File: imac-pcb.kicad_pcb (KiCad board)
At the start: 2 copper layers, 43 parts, among them P2 PATCHBAY_IO, P5 INPUTS, P7 PWR_X3, Q1 NX3008N***, Q2 PMV48XP, Q3 NX3008N***, Q4 NX3008N***, U1 MCP6004, U2 MCP6004, U3 NCP4620, U4 ADG849

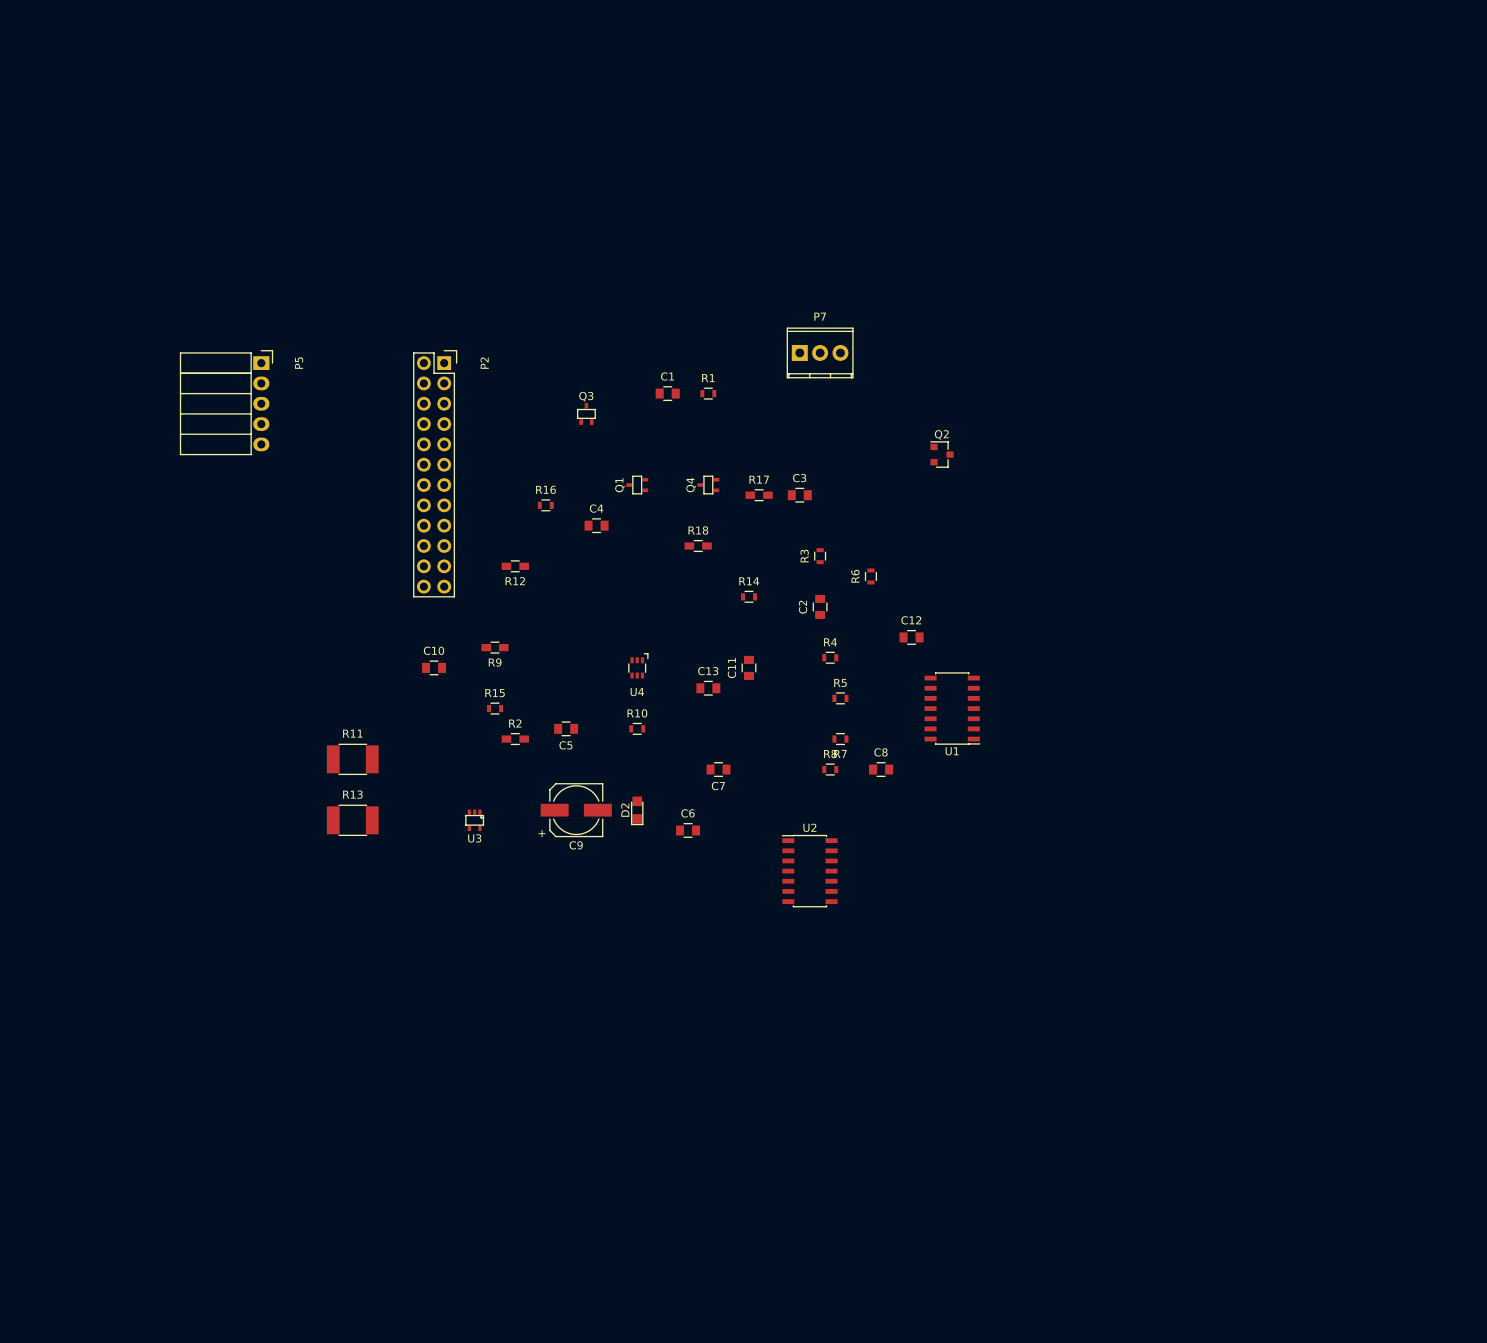
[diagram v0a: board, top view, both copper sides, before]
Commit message: begin layout of pcb
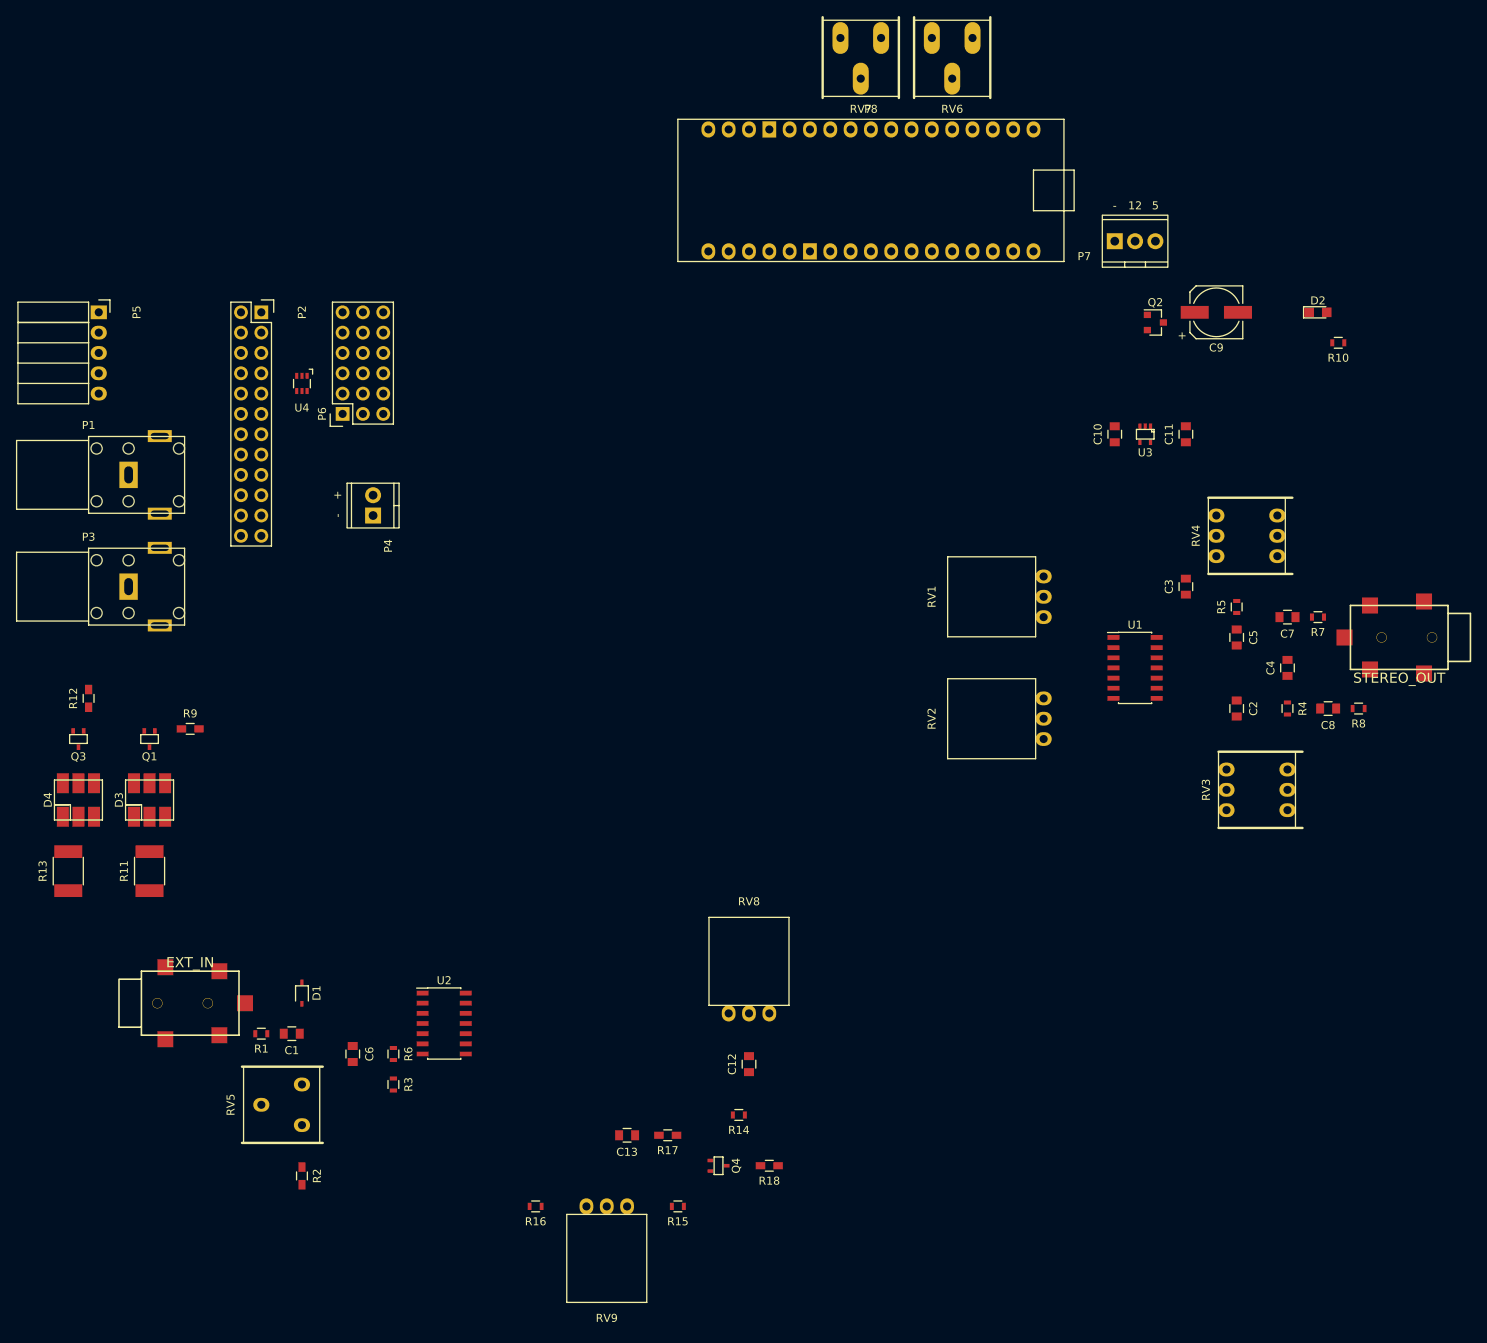
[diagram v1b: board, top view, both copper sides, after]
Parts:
- added D1: 1N4148, Imac:SOD-323F, F.Cu at (114.3, 151.1)
- added D3: CLP6B-WKW, Imac:PLCC6-3in1-SMD-LED, F.Cu at (95.2, 127.0)
- added D4: CLP6B-WKW, Imac:PLCC6-3in1-SMD-LED, F.Cu at (86.4, 127.0)
- added J1: EXT_IN, Lumberg:Lumberg_1503_03, F.Cu at (100.3, 152.4)
- added J2: STEREO_OUT, Lumberg:Lumberg_1503_03, F.Cu at (251.5, 106.7)
- added P1: PROBE1, Imac:PSG01546_RCA_Phono_Connector, F.Cu at (87.6, 86.4)
- added P3: PROBE2, Imac:PSG01546_RCA_Phono_Connector, F.Cu at (87.6, 100.3)
- added P4: EXT_OUT, Imac:TerminalBlock_TE_282834-2-2.54mm_2pol, F.Cu at (123.2, 91.4)
- added P6: PATCHBAY_A, Imac:Socket_Strip_Straight_3x06, F.Cu at (119.4, 78.7)
- added P8: ARDUINO_MICRO, Imac:Arduino_Micro_2x1x17, F.Cu at (165.1, 43.2)
- added RV1: 100k, Imac:Pot_Bourns_PTV09A-4_Horizontal_Rear_mount, F.Cu at (207.0, 104.1)
- added RV2: 100k, Imac:Pot_Bourns_PTV09A-4_Horizontal_Rear_mount, F.Cu at (207.0, 119.4)
- added RV3: 100k, Imac:Dual_Pot_Bourns_3301H-00X, F.Cu at (229.9, 128.3)
- added RV4: 100k, Imac:Dual_Pot_Bourns_3301H-00X, F.Cu at (228.6, 96.5)
- added RV5: 100k**, Imac:Trimpot_Bourns_3386F_Vishay_M63, F.Cu at (114.3, 167.6)
- added RV6: 100k†, Imac:Trimpot_Bourns_Big_Pads_3386F_Vishay_M63, F.Cu at (198.1, 31.8)
- added RV7: 100k†, Imac:Trimpot_Bourns_Big_Pads_3386F_Vishay_M63, F.Cu at (186.7, 31.8)
- added RV8: 100k, Imac:Pot_Bourns_PTV09A-4_Horizontal_Rear_mount, F.Cu at (167.6, 153.7)
- added RV9: 100k, Imac:Pot_Bourns_PTV09A-4_Horizontal_Rear_mount, F.Cu at (154.9, 177.8)
- P7: footprint Terminal_Blocks:TerminalBlock_Pheonix_MPT-2.54mm_3pol -> Imac:TerminalBlock_TE_282834-3-2.54mm_3pol
- moved D2 105.4 mm to (241.3, 66.0), turned to 0 degrees
- moved C9 101.4 mm to (228.6, 66.0)
- moved R10 100.0 mm to (243.8, 69.8), turned to 180 degrees
- moved R1 97.6 mm to (109.2, 156.2), turned to 180 degrees
- moved U3 96.7 mm to (219.7, 81.3)
- moved C1 92.8 mm to (113.0, 156.2), turned to 180 degrees
- moved C10 90.0 mm to (215.9, 81.3), turned to 90 degrees
- moved C4 88.2 mm to (237.5, 110.5), turned to 90 degrees
- moved R16 87.6 mm to (143.5, 177.8), turned to 180 degrees
- moved Q4 85.1 mm to (166.4, 172.7), turned to 270 degrees
- moved R3 84.9 mm to (125.7, 162.6), turned to 270 degrees
- moved C5 84.6 mm to (231.1, 106.7), turned to 270 degrees
- moved R6 84.4 mm to (125.7, 158.8), turned to 270 degrees
- moved R17 80.8 mm to (160.0, 168.9), turned to 180 degrees
- moved R18 78.0 mm to (172.7, 172.7), turned to 180 degrees
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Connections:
- P2 pad 1: /PB1 -> /AUDIOA_SEND
- P2 pad 10: /D6 -> /IN3
- P2 pad 11: GND -> /AUDIOB_SEND
- P2 pad 12: GND -> /IN4
- P2 pad 13: /AUDIOA_SEND -> /LED_CTRL1
- P2 pad 14: /AUDIOA_SEND -> /IN5
- P2 pad 15: /AUDIOA_SEND -> /LED_CTRL2
- P2 pad 16: /AUDIOB_SEND -> /EXT_IN
- P2 pad 17: /AUDIOB_SEND -> /EXT_OUT
- P2 pad 18: /AUDIOB_SEND -> /D3
- P2 pad 19: /LED_CTRL1 -> /A0_IN
- P2 pad 2: /PB2 -> /PB1
- P2 pad 20: /LED_CTRL2 -> /D6
- P2 pad 21: /EXT_OUT -> GND
- P2 pad 22: /A0_IN -> GND
- P2 pad 3: /IN1 -> /AUDIOA_SEND
- P2 pad 4: /IN2 -> /PB2
- P2 pad 5: /IN3 -> /AUDIOA_SEND
- P2 pad 6: /IN4 -> /IN1
- P2 pad 7: /IN5 -> /AUDIOB_SEND
- P2 pad 8: /EXT_IN -> /IN2
- P2 pad 9: /D3 -> /AUDIOB_SEND

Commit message: major work on PCB layout
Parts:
- removed P8: ARDUINO_MICRO, Imac:Arduino_Micro_2x1x17
- added C14: 1u, Capacitors_SMD:C_0805, F.Cu at (71.8, -0.64)
- added C15: 100n, Capacitors_SMD:C_0805, F.Cu at (68.6, -0.64)
- added C16: 100n, Capacitors_SMD:C_0805, F.Cu at (83.8, -0.64)
- added C17: 1u, Capacitors_SMD:C_0805, F.Cu at (87.0, -0.64)
- added C18: 22u, Imac:2917C, F.Cu at (62.9, -0.64)
- added C19: 100n, Capacitors_SMD:C_0805, F.Cu at (64.3, 34.9)
- added C20: 100n, Capacitors_SMD:C_0805, F.Cu at (31.4, 16.4)
- added D5: CLP6B-WKW, Imac:PLCC6-3in1-SMD-LED, F.Cu at (43.3, 40.5)
- added R19: 27****, Resistors_SMD:R_1812_HandSoldering, F.Cu at (43.4, 34.6)
- added SW1: RESET_SW, Imac:EVQ_BUT, F.Cu at (66.7, 14.3)
- added U5: arduino_pro_micro, Imac:arduino_pro_micro, F.Cu at (74.3, -0.64)
- added U6: NCP1117-5, TO_SOT_Packages_SMD:SOT-223, F.Cu at (77.5, -0.64)
- C6: footprint Capacitors_SMD:C_0805 -> Capacitors_SMD:C_0805_HandSoldering
- D3, D4: moved to B.Cu
- Q1, Q3, Q4: footprint TO_SOT_Packages_SMD:SC-70 -> imac:SC-70-BIG-PADS
- R1, R10, R14, R15, R16, R3, R4, R5, R6, R7, R8: footprint Resistors_SMD:R_0603 -> Resistors_SMD:R_0805
- R11: value 27 -> 27****; footprint Resistors_SMD:R_1812 -> Resistors_SMD:R_1812_HandSoldering
- R12, R17, R18, R2, R9: footprint Resistors_SMD:R_0603_HandSoldering -> Resistors_SMD:R_0805_HandSoldering
- U2: value MCP6004 -> MCP6002; footprint Housings_SOIC:SOIC-14_3.9x8.7mm_Pitch1.27mm -> Imac:SOIC-8_3.9x4.9mm_Pitch1.27mm_handsolder
- moved RV9 226.8 mm to (5.08, 7.62), turned to 90 degrees
- moved R15 219.1 mm to (20.8, 9.75), turned to 270 degrees
- moved RV8 210.3 mm to (5.08, 20.3), turned to 90 degrees
- moved R16 209.4 mm to (18.5, 9.75), turned to 270 degrees
- moved R14 208.8 mm to (22.5, 17.5), turned to 90 degrees
- moved C12 207.1 mm to (19.9, 17.5)
- moved C13 205.5 mm to (20.8, 13.2), turned to 270 degrees
- moved R10 203.6 mm to (52.7, -0.24), turned to 90 degrees
- moved D2 202.7 mm to (49.8, -0.26), turned to 90 degrees
- moved C11 202.0 mm to (37.0, 6.75)
- moved R18 201.1 mm to (38.8, 22.8), turned to 90 degrees
- moved Q4 200.6 mm to (33.5, 22.5), turned to 0 degrees
- moved RV3 199.6 mm to (58.4, 26.0), turned to 180 degrees
- moved R8 197.7 mm to (72.1, 22.2), turned to 270 degrees
- moved R17 196.6 mm to (28.5, 22.8), turned to 270 degrees
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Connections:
- D3 pad 1: Net-(D3-Pad1) -> 5V_SYS
- D3 pad 2: Net-(D3-Pad1) -> 5V_SYS
- D3 pad 3: Net-(D3-Pad1) -> 5V_SYS
- D4 pad 1: Net-(D4-Pad1) -> 5V_SYS
- D4 pad 2: Net-(D4-Pad1) -> 5V_SYS
- D4 pad 3: Net-(D4-Pad1) -> 5V_SYS
- P6 pad 1: /SWA_COM -> /SWA_NO
- P6 pad 2: /SWA_COM -> /SWA_NO
- P6 pad 3: /SWA_COM -> /SWA_NO
- P6 pad 4: /SWA_NC -> /SWA_COM
- P6 pad 5: /SWA_NC -> /SWA_COM
- P6 pad 6: /SWA_NC -> /SWA_COM
- P6 pad 7: /SWA_NO -> /SWA_NC
- P6 pad 8: /SWA_NO -> /SWA_NC
- P6 pad 9: /SWA_NO -> /SWA_NC
- Q1 pad 3: Net-(D3-Pad4) -> Net-(Q1-Pad3)
- Q3 pad 3: Net-(D4-Pad4) -> Net-(Q3-Pad3)
- R11 pad 1: 5V_SYS -> Net-(D3-Pad4)
- R11 pad 2: Net-(D3-Pad1) -> Net-(Q1-Pad3)
- R13 pad 1: 5V_SYS -> Net-(D4-Pad4)
- R13 pad 2: Net-(D4-Pad1) -> Net-(Q3-Pad3)
- U1 pad 1: Net-(RV3-Pad1) -> Net-(C2-Pad1)
- U1 pad 10: Net-(C4-Pad1) -> Net-(RV2-Pad2)
- U1 pad 2: Net-(RV3-Pad1) -> Net-(C2-Pad1)
- U1 pad 3: Net-(RV1-Pad2) -> Net-(C4-Pad1)
- U1 pad 5: Net-(RV2-Pad2) -> Net-(RV1-Pad2)
- U1 pad 6: Net-(RV4-Pad1) -> Net-(RV3-Pad1)
- U1 pad 7: Net-(RV4-Pad1) -> Net-(RV3-Pad1)
- U1 pad 8: Net-(C2-Pad1) -> Net-(RV4-Pad1)
- U1 pad 9: Net-(C2-Pad1) -> Net-(RV4-Pad1)
- U2 pad 4: 5V_SYS -> GND
- U2 pad 8: (no net) -> 5V_SYS
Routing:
- net 5V_SYS: track 0.00 -> 250.7 mm, vias 0 -> 2
- net Net-(Q1-Pad3): track 0.00 -> 36.5 mm
- net 2V5_REF: track 0.00 -> 28.3 mm
- net Net-(C1-Pad1): track 0.00 -> 26.7 mm
- net Net-(C3-Pad2): track 0.00 -> 26.0 mm
- net 12V_IN: track 0.00 -> 24.9 mm
- net Net-(C6-Pad2): track 0.00 -> 23.9 mm
- net Net-(SW1-Pad2): track 0.00 -> 22.8 mm
- net Net-(R2-Pad1): track 0.00 -> 20.0 mm
- net Net-(C2-Pad2): track 0.00 -> 18.8 mm
- net Net-(Q1-Pad1): track 0.00 -> 18.3 mm
- net Net-(RV4-Pad1): track 0.00 -> 17.1 mm
- net /MOD_OUT: track 0.00 -> 16.0 mm
- net Net-(RV2-Pad2): track 0.00 -> 14.1 mm, vias 0 -> 2
- net Net-(RV3-Pad1): track 0.00 -> 14.0 mm, vias 0 -> 2
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- added copper zone on B.Cu, net GND
- added copper zone on F.Cu, net GND
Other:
- board outline added: 90 x 60 mm
- net class Ground-Big: trace_width 0.35 -> 0.4; via_dia 0.6 -> 0.8
- net class Power: trace_width 0.3 -> 0.4; via_dia 0.6 -> 0.8
- board text added: "TODO: - make a hand solderable version of the SOIC14 chip - make a hand solderable mosfet version"
